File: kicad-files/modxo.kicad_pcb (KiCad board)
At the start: 2 copper layers, 40 x 30 mm, 10 parts, among them J1 Conn_02x06_Odd_Even, J2 Conn_01x01_Pin, SW1 SW_DPDT_x2, U1 rp2040-zero

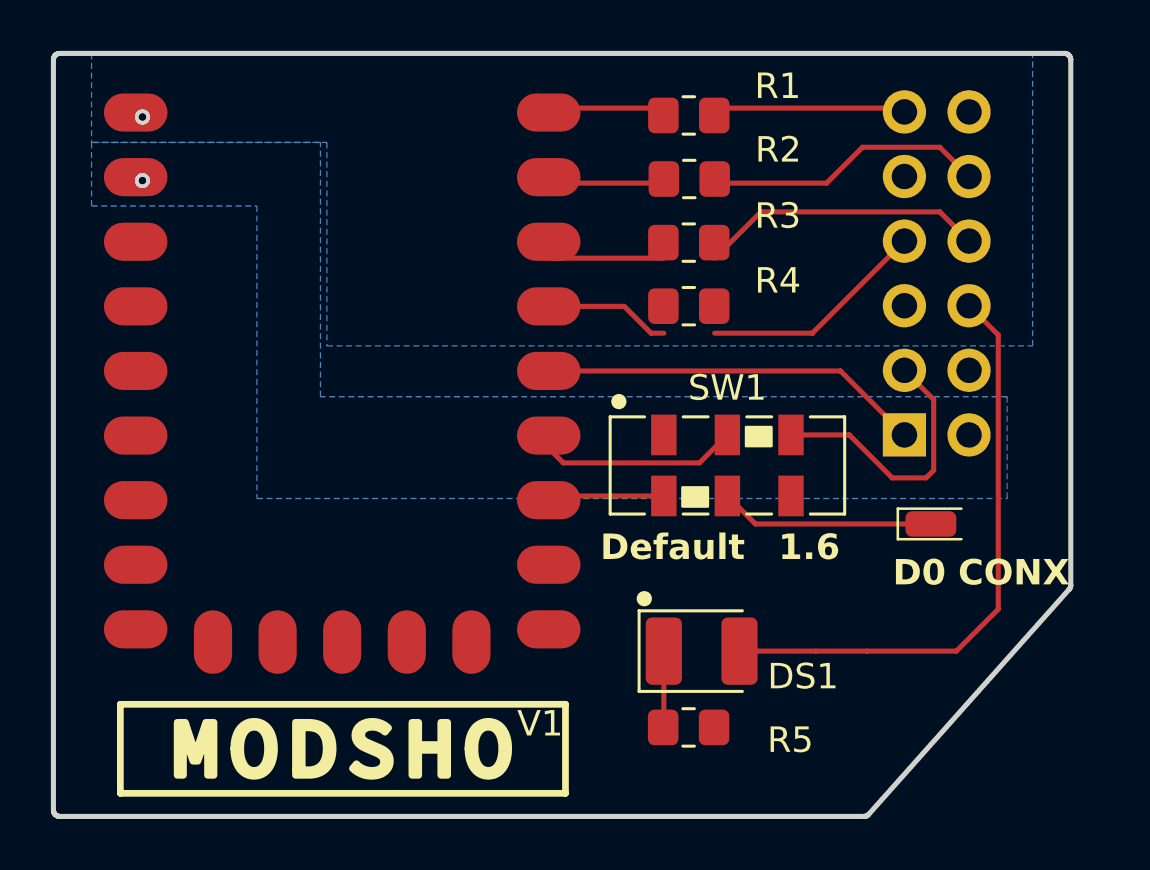
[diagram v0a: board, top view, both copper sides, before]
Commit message: Minor usability improvements
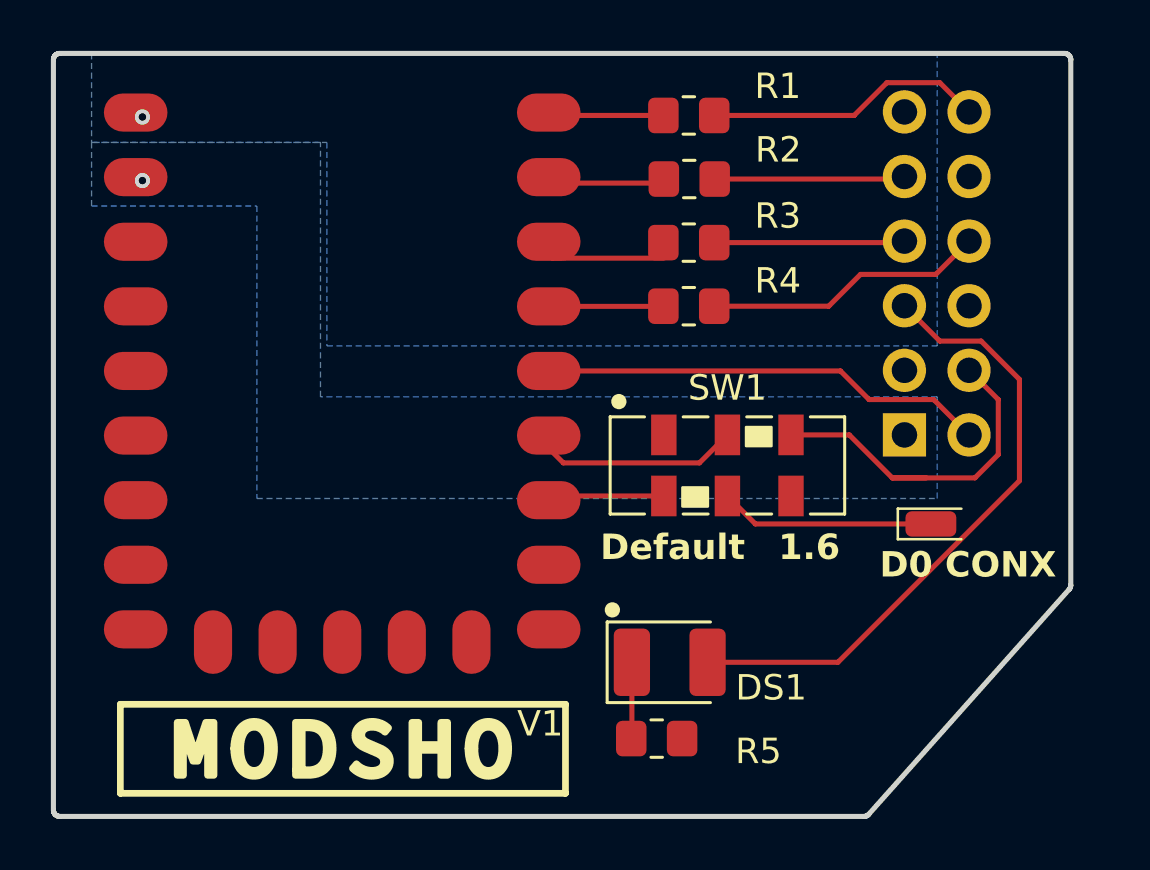
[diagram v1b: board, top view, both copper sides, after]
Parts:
- moved DS1 1.33 mm to (134.2, 88.8)
- moved R5 1.33 mm to (133.7, 91.8)
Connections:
- J1 pad 1: LCLK -> GND
- J1 pad 10: LAD1 -> unconnected-(J1-Pin_10-Pad10)
- J1 pad 11: LAD0 -> unconnected-(J1-Pin_11-Pad11)
- J1 pad 12: unconnected-(J1-Pin_12-Pad12) -> LAD0
- J1 pad 2: GND -> LCLK
- J1 pad 3: LFRAME -> unconnected-(J1-Pin_3-Pad3)
- J1 pad 4: unconnected-(J1-Pin_4-Pad4) -> LFRAME
- J1 pad 5: unconnected-(J1-Pin_5-Pad5) -> +5V
- J1 pad 6: +5V -> unconnected-(J1-Pin_6-Pad6)
- J1 pad 7: LAD3 -> LAD2
- J1 pad 8: LAD2 -> LAD3
- J1 pad 9: unconnected-(J1-Pin_9-Pad9) -> LAD1
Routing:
- net LAD2: track 11.2 -> 7.50 mm
- net +5V: track 22.0 -> 25.6 mm
- net LAD1: track 11.1 -> 7.50 mm
- net LFRAME: track 10.8 -> 14.3 mm
- net LAD0: track 7.52 -> 11.0 mm
- net LAD3: track 8.96 -> 11.1 mm
- net LCLK: track 16.0 -> 18.1 mm
